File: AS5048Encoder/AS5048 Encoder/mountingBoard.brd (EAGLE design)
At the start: 48.8 x 30 mm, 0 parts

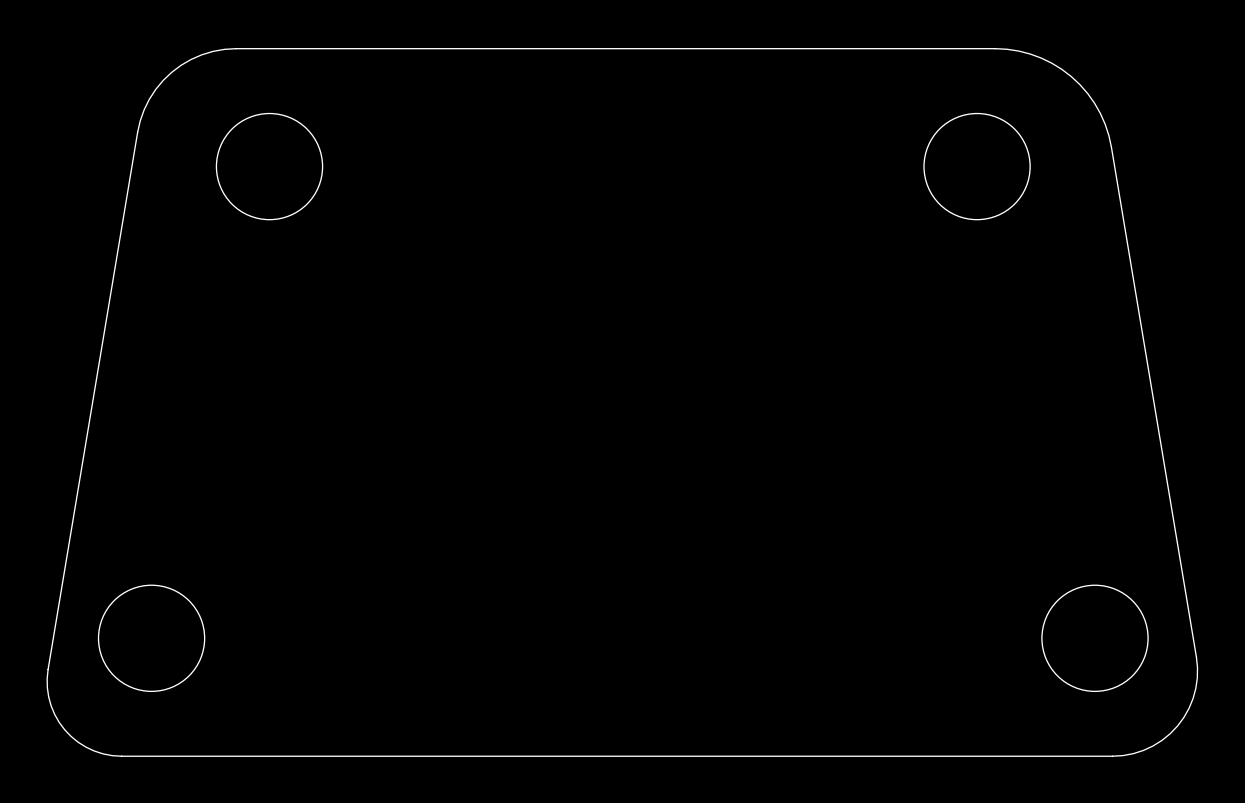
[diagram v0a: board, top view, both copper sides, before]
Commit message: total revamp of encoder board
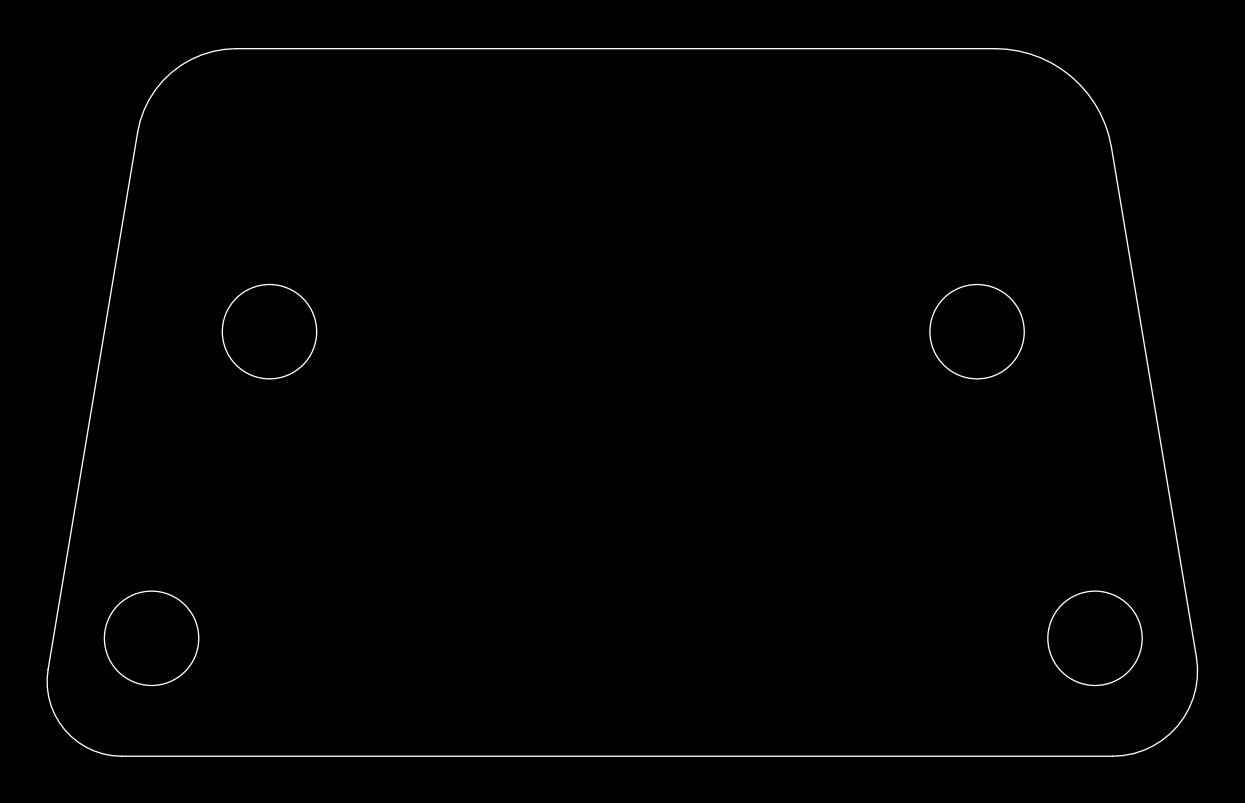
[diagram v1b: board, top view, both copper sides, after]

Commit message: shipped here
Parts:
- added U$1, U$2: TERMINALBLOCK277-1667-ND, makesmith:TERMINALBLOCK277-1667-ND
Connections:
- new net GND: U$1.2, U$2.2
- new net PWR: U$1.1, U$2.1
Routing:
- added copper zone on layer 16, net GND
- added copper zone on layer 1, net PWR
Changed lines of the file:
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@@
 <setting verticaltext="up"/>
 </settings>
-<grid distance="1" unitdist="mm" unit="mm" style="lines" multiple="1" display="no" altdistance="0.025" altunitdist="inch" altunit="inch"/>
+<grid distance="39.3700787" unitdist="mil" unit="mil" style="lines" multiple="1" display="no" altdistance="0.025" altunitdist="inch" altunit="inch"/>
 <layers>
 <layer number="1" name="Top" color="4" fill="1" visible="yes" active="yes"/>
@@
 </autorouter>
 <elements>
+<element name="U$1" library="makesmith" package="TERMINALBLOCK277-1667-ND" value="TERMINALBLOCK277-1667-ND" x="18" y="26"/>
+<element name="U$2" library="makesmith" package="TERMINALBLOCK277-1667-ND" value="TERMINALBLOCK277-1667-ND" x="32" y="26"/>
 </elements>
 <signals>
+<signal name="GND">
+<contactref element="U$1" pad="2"/>
+<contactref element="U$2" pad="2"/>
+<polygon width="0.4064" layer="16">
+<vertex x="13" y="22"/>
+<vertex x="13" y="30"/>
+<vertex x="37" y="30"/>
+<vertex x="37" y="22"/>
+</polygon>
+</signal>
+<signal name="PWR">
+<contactref element="U$1" pad="1"/>
+<contactref element="U$2" pad="1"/>
+<polygon width="0.4064" layer="1">
+<vertex x="13" y="22"/>
+<vertex x="13" y="30"/>
+<vertex x="37" y="30"/>
+<vertex x="37" y="22"/>
+</polygon>
+</signal>
 </signals>
 </board>
